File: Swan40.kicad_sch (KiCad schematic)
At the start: 82 parts, among them SW1 SW_PUSH, SW10 SW_PUSH, SW11 SW_PUSH, SW12 SW_PUSH, SW13 SW_PUSH, SW14 SW_PUSH, SW15 SW_PUSH, SW16 SW_PUSH, SW17 SW_PUSH, SW18 SW_PUSH, SW19 SW_PUSH, SW2 SW_PUSH, SW20 SW_PUSH, SW21 SW_PUSH, SW22 SW_PUSH, SW23 SW_PUSH, SW24 SW_PUSH, SW25 SW_PUSH, SW26 SW_PUSH, SW27 SW_PUSH, SW28 SW_PUSH, SW29 SW_PUSH, SW3 SW_PUSH, SW30 SW_PUSH, SW31 SW_PUSH, SW32 SW_PUSH, SW33 SW_PUSH, SW34 SW_PUSH, SW35 SW_PUSH, SW36 SW_PUSH, SW37 SW_PUSH, SW38 SW_PUSH, SW39 SW_PUSH, SW4 SW_PUSH, SW40 SW_PUSH, SW5 SW_PUSH, SW6 SW_PUSH, SW7 SW_PUSH, SW8 SW_PUSH, SW9 SW_PUSH, U1 xiao_nrf52840, U2 xiao_nrf52840

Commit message: Semi-broken 1st attempt
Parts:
- added H1, H3: BAT+, kbd:1pin_conn, symbol Mechanical:MountingHole_Pad
- added H2, H4: BAT-, kbd:1pin_conn, symbol Mechanical:MountingHole_Pad
- added SW17, SW34: SW_DPDT_x2, MSK-12C02:MSK-12C02, symbol Switch:SW_DPDT_x2
- added TP1, TP3: BOARD+, kbd:1pad_conn_board, symbol Connector:TestPoint
- added TP2, TP4: BOARD-, kbd:1pad_conn_board, symbol Connector:TestPoint
- renumbered SW17 to SW18, SW18 to SW19, SW19 to SW20, SW20 to SW21, SW21 to SW22, SW22 to SW23, SW23 to SW24, SW24 to SW25, SW25 to SW26, SW26 to SW27, SW27 to SW28, SW28 to SW29, SW29 to SW30, SW30 to SW31, SW31 to SW32, SW32 to SW33, SW33 to SW35, SW34 to SW36, SW35 to SW37, SW36 to SW38, SW37 to SW39, SW38 to SW40, SW39 to SW41, SW40 to SW42
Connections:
- net LCOL1: now also U1.3 (PA10_A2_D2); no longer U1.1 (PA02_A0_D0)
- net LCOL2: now also U1.4 (PA11_A3_D3); no longer U1.2 (PA4_A1_D1)
- net LCOL3: now also U1.5 (PA8_A4_D4_SDA); no longer U1.3 (PA10_A2_D2)
- net LCOL4: now also U1.6 (PA9_A5_D5_SCL); no longer U1.4 (PA11_A3_D3)
- net RCOL1: now also U2.3 (PA10_A2_D2); no longer U2.1 (PA02_A0_D0)
- net RCOL2: now also U2.4 (PA11_A3_D3); no longer U2.2 (PA4_A1_D1)
- net RCOL3: now also U2.5 (PA8_A4_D4_SDA); no longer U2.3 (PA10_A2_D2)
- net RCOL4: now also U2.6 (PA9_A5_D5_SCL); no longer U2.4 (PA11_A3_D3)
- new net: H4.1, TP4.1
- new net: SW34.3 (C), TP3.1
- new net: H3.1, SW34.2 (B)
- new net: H1.1, SW17.2 (B)
- new net: H2.1, TP2.1
- new net: SW17.3 (C), TP1.1
- no-connect marks 0 -> 13

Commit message: Base wiring completed
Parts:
- U1, U2: footprint xiao_nrf52840:xiao_nrf52840 -> xiao_nrf52840:xiao_nrf52840_v2
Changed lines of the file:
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@@
       (effects (font (size 1.27 1.27)))
     )
-    (property "Footprint" "xiao_nrf52840:xiao_nrf52840" (at 43.18 60.96 0)
+    (property "Footprint" "xiao_nrf52840:xiao_nrf52840_v2" (at 43.18 60.96 0)
       (effects (font (size 1.27 1.27)) hide)
     )
@@
       (effects (font (size 1.27 1.27)))
     )
-    (property "Footprint" "xiao_nrf52840:xiao_nrf52840" (at 232.41 58.42 0)
-      (effects (font (size 1.27 1.27)) hide)
-    )
+    (property "Footprint" "xiao_nrf52840:xiao_nrf52840_v2" (at 232.41 58.42 0)
+      (effects (font (size 1.27 1.27)) hide)
+    )

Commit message: Wiring complete
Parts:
- removed H1, H3: BAT+, kbd:1pin_conn, symbol Mechanical:MountingHole_Pad
- removed H2, H4: BAT-, kbd:1pin_conn, symbol Mechanical:MountingHole_Pad
- added TP1, TP5: BAT+, kbd:1pad_conn_board, symbol Connector:TestPoint
- added TP2, TP6: BAT-, kbd:1pad_conn_board, symbol Connector:TestPoint
- renumbered TP1 to TP3, TP2 to TP4, TP3 to TP7, TP4 to TP8
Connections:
- net at TP8.1: now also TP6.1
- net at SW34.2 (B): now also TP5.1
- net at SW17.2 (B): now also TP1.1
- net at TP4.1: now also TP2.1
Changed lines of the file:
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@@
+    )
+  )
+  (symbol (lib_id "Connector:TestPoint") (at 292.1 55.88 90) (unit 1)
+    (in_bom yes) (on_board yes) (dnp no) (fields_autoplaced)
+    (property "Reference" "TP5" (at 288.798 50.8 90)
+      (effects (font (size 1.27 1.27)))
+    )
+    (property "Value" "BAT+" (at 288.798 53.34 90)
+      (effects (font (size 1.27 1.27)))
+    )
+    (property "Footprint" "kbd:1pad_conn_board" (at 292.1 50.8 0)
+      (effects (font (size 1.27 1.27)) hide)
+    )
+    (property "Datasheet" "~" (at 292.1 50.8 0)
+      (effects (font (size 1.27 1.27)) hide)
+    )
+    (pin "1")
+    (instances
+      (project "Swan40"
+        (path "/b7a22810-d1fc-438f-bfc5-8d77c3380840"
+          (reference "TP5") (unit 1)
+        )
+      )
     )
   )
@@
     )
   )
-  (symbol (lib_id "Mechanical:MountingHole_Pad") (at 289.56 71.12 90) (unit 1)
-    (in_bom yes) (on_board yes) (dnp no) (fields_autoplaced)
-    (property "Reference" "H4" (at 288.29 64.77 90)
-      (effects (font (size 1.27 1.27)))
-    )
-    (property "Value" "BAT-" (at 288.29 67.31 90)
-      (effects (font (size 1.27 1.27)))
-    )
-    (property "Footprint" "kbd:1pin_conn" (at 289.56 71.12 0)
-      (effects (font (size 1.27 1.27)) hide)
-    )
-    (property "Datasheet" "~" (at 289.56 71.12 0)
-      (effects (font (size 1.27 1.27)) hide)
-    )
-    (pin "1")
-    (instances
-      (project "Swan40"
-        (path "/b7a22810-d1fc-438f-bfc5-8d77c3380840"
-          (reference "H4") (unit 1)
-        )
-      )
-    )
-  )
   (symbol (lib_id "kbd:SW_PUSH") (at 283.21 119.38 0) (unit 1)
     (in_bom yes) (on_board yes) (dnp no) (fields_autoplaced)
@@
     )
   )
+  (symbol (lib_id "Connector:TestPoint") (at 292.1 71.12 90) (unit 1)
+    (in_bom yes) (on_board yes) (dnp no) (fields_autoplaced)
+    (property "Reference" "TP6" (at 288.798 66.04 90)
+      (effects (font (size 1.27 1.27)))
+    )
+    (property "Value" "BAT-" (at 288.798 68.58 90)
+      (effects (font (size 1.27 1.27)))
+    )
+    (property "Footprint" "kbd:1pad_conn_board" (at 292.1 66.04 0)
+      (effects (font (size 1.27 1.27)) hide)
+    )
+    (property "Datasheet" "~" (at 292.1 66.04 0)
+      (effects (font (size 1.27 1.27)) hide)
+    )
+    (pin "1")
+    (instances
+      (project "Swan40"
+        (path "/b7a22810-d1fc-438f-bfc5-8d77c3380840"
+          (reference "TP6") (unit 1)
+        )
+      )
+    )
+  )
   (symbol (lib_id "Device:D") (at 86.36 111.76 90) (unit 1)
     (in_bom yes) (on_board yes) (dnp no) (fields_autoplaced)
@@
   (symbol (lib_id "Connector:TestPoint") (at 302.26 58.42 270) (unit 1)
     (in_bom yes) (on_board yes) (dnp no) (fields_autoplaced)
-    (property "Reference" "TP3" (at 307.34 57.15 90)
+    (property "Reference" "TP7" (at 307.34 57.15 90)
       (effects (font (size 1.27 1.27)) (justify left))
     )
@@
       (project "Swan40"
         (path "/b7a22810-d1fc-438f-bfc5-8d77c3380840"
-          (reference "TP3") (unit 1)
+          (reference "TP7") (unit 1)
         )
       )
@@
         (path "/b7a22810-d1fc-438f-bfc5-8d77c3380840"
           (reference "D27") (unit 1)
+        )
+      )
+    )
+  )
+  (symbol (lib_id "Connector:TestPoint") (at 114.3 74.93 90) (unit 1)
+    (in_bom yes) (on_board yes) (dnp no) (fields_autoplaced)
+    (property "Reference" "TP2" (at 110.998 69.85 90)
+      (effects (font (size 1.27 1.27)))
+    )
+    (property "Value" "BAT-" (at 110.998 72.39 90)
+      (effects (font (size 1.27 1.27)))
+    )
+    (property "Footprint" "kbd:1pad_conn_board" (at 114.3 69.85 0)
+      (effects (font (size 1.27 1.27)) hide)
+    )
+    (property "Datasheet" "~" (at 114.3 69.85 0)
+      (effects (font (size 1.27 1.27)) hide)
+    )
+    (pin "1")
+    (instances
+      (project "Swan40"
+        (path "/b7a22810-d1fc-438f-bfc5-8d77c3380840"
+          (reference "TP2") (unit 1)
         )
       )
@@
     )
   )
-  (symbol (lib_id "Mechanical:MountingHole_Pad") (at 289.56 55.88 90) (unit 1)
-    (in_bom yes) (on_board yes) (dnp no) (fields_autoplaced)
-    (property "Reference" "H3" (at 288.29 49.53 90)
-      (effects (font (size 1.27 1.27)))
-    )
-    (property "Value" "BAT+" (at 288.29 52.07 90)
-      (effects (font (size 1.27 1.27)))
-    )
-    (property "Footprint" "kbd:1pin_conn" (at 289.56 55.88 0)
-      (effects (font (size 1.27 1.27)) hide)
-    )
-    (property "Datasheet" "~" (at 289.56 55.88 0)
-      (effects (font (size 1.27 1.27)) hide)
-    )
-    (pin "1")
-    (instances
-      (project "Swan40"
-        (path "/b7a22810-d1fc-438f-bfc5-8d77c3380840"
-          (reference "H3") (unit 1)
-        )
-      )
-    )
-  )
   (symbol (lib_id "kbd:SW_PUSH") (at 300.99 105.41 0) (unit 1)
     (in_bom yes) (on_board yes) (dnp no) (fields_autoplaced)
@@
         (path "/b7a22810-d1fc-438f-bfc5-8d77c3380840"
           (reference "SW1") (unit 1)
-        )
-      )
-    )
-  )
-  (symbol (lib_id "Mechanical:MountingHole_Pad") (at 111.76 59.69 90) (unit 1)
-    (in_bom yes) (on_board yes) (dnp no) (fields_autoplaced)
-    (property "Reference" "H1" (at 110.49 53.34 90)
-      (effects (font (size 1.27 1.27)))
-    )
-    (property "Value" "BAT+" (at 110.49 55.88 90)
-      (effects (font (size 1.27 1.27)))
-    )
-    (property "Footprint" "kbd:1pin_conn" (at 111.76 59.69 0)
-      (effects (font (size 1.27 1.27)) hide)
-    )
-    (property "Datasheet" "~" (at 111.76 59.69 0)
-      (effects (font (size 1.27 1.27)) hide)
-    )
-    (pin "1")
-    (instances
-      (project "Swan40"
-        (path "/b7a22810-d1fc-438f-bfc5-8d77c3380840"
-          (reference "H1") (unit 1)
         )
       )
@@
   (symbol (lib_id "Connector:TestPoint") (at 124.46 74.93 270) (unit 1)
     (in_bom yes) (on_board yes) (dnp no) (fields_autoplaced)
-    (property "Reference" "TP2" (at 129.54 73.66 90)
+    (property "Reference" "TP4" (at 129.54 73.66 90)
       (effects (font (size 1.27 1.27)) (justify left))
     )
@@
       (project "Swan40"
         (path "/b7a22810-d1fc-438f-bfc5-8d77c3380840"
-          (reference "TP2") (unit 1)
+          (reference "TP4") (unit 1)
         )
       )
@@
   (symbol (lib_id "Connector:TestPoint") (at 124.46 62.23 270) (unit 1)
     (in_bom yes) (on_board yes) (dnp no) (fields_autoplaced)
-    (property "Reference" "TP1" (at 129.54 60.96 90)
+    (property "Reference" "TP3" (at 129.54 60.96 90)
       (effects (font (size 1.27 1.27)) (justify left))
     )
@@
       (project "Swan40"
         (path "/b7a22810-d1fc-438f-bfc5-8d77c3380840"
-          (reference "TP1") (unit 1)
+          (reference "TP3") (unit 1)
         )
       )
@@
     )
   )
+  (symbol (lib_id "Connector:TestPoint") (at 114.3 59.69 90) (unit 1)
+    (in_bom yes) (on_board yes) (dnp no) (fields_autoplaced)
+    (property "Reference" "TP1" (at 110.998 54.61 90)
+      (effects (font (size 1.27 1.27)))
+    )
+    (property "Value" "BAT+" (at 110.998 57.15 90)
+      (effects (font (size 1.27 1.27)))
+    )
+    (property "Footprint" "kbd:1pad_conn_board" (at 114.3 54.61 0)
+      (effects (font (size 1.27 1.27)) hide)
+    )
+    (property "Datasheet" "~" (at 114.3 54.61 0)
+      (effects (font (size 1.27 1.27)) hide)
+    )
+    (pin "1")
+    (instances
+      (project "Swan40"
+        (path "/b7a22810-d1fc-438f-bfc5-8d77c3380840"
+          (reference "TP1") (unit 1)
+        )
+      )
+    )
+  )
   (symbol (lib_id "kbd:SW_PUSH") (at 265.43 133.35 0) (unit 1)
     (in_bom yes) (on_board yes) (dnp no) (fields_autoplaced)
@@
     )
   )
-  (symbol (lib_id "Mechanical:MountingHole_Pad") (at 111.76 74.93 90) (unit 1)
-    (in_bom yes) (on_board yes) (dnp no) (fields_autoplaced)
-    (property "Reference" "H2" (at 110.49 68.58 90)
-      (effects (font (size 1.27 1.27)))
-    )
-    (property "Value" "BAT-" (at 110.49 71.12 90)
-      (effects (font (size 1.27 1.27)))
-    )
-    (property "Footprint" "kbd:1pin_conn" (at 111.76 74.93 0)
-      (effects (font (size 1.27 1.27)) hide)
-    )
-    (property "Datasheet" "~" (at 111.76 74.93 0)
-      (effects (font (size 1.27 1.27)) hide)
-    )
-    (pin "1")
-    (instances
-      (project "Swan40"
-        (path "/b7a22810-d1fc-438f-bfc5-8d77c3380840"
-          (reference "H2") (unit 1)
-        )
-      )
-    )
-  )
   (symbol (lib_id "Device:D") (at 86.36 139.7 90) (unit 1)
     (in_bom yes) (on_board yes) (dnp no) (fields_autoplaced)
@@
   (symbol (lib_id "Connector:TestPoint") (at 302.26 71.12 270) (unit 1)
     (in_bom yes) (on_board yes) (dnp no) (fields_autoplaced)
-    (property "Reference" "TP4" (at 307.34 69.85 90)
+    (property "Reference" "TP8" (at 307.34 69.85 90)
       (effects (font (size 1.27 1.27)) (justify left))
     )
@@
       (project "Swan40"
         (path "/b7a22810-d1fc-438f-bfc5-8d77c3380840"
-          (reference "TP4") (unit 1)
-        )
-      )
+          (reference "TP8") (unit 1)
+        )
+      )

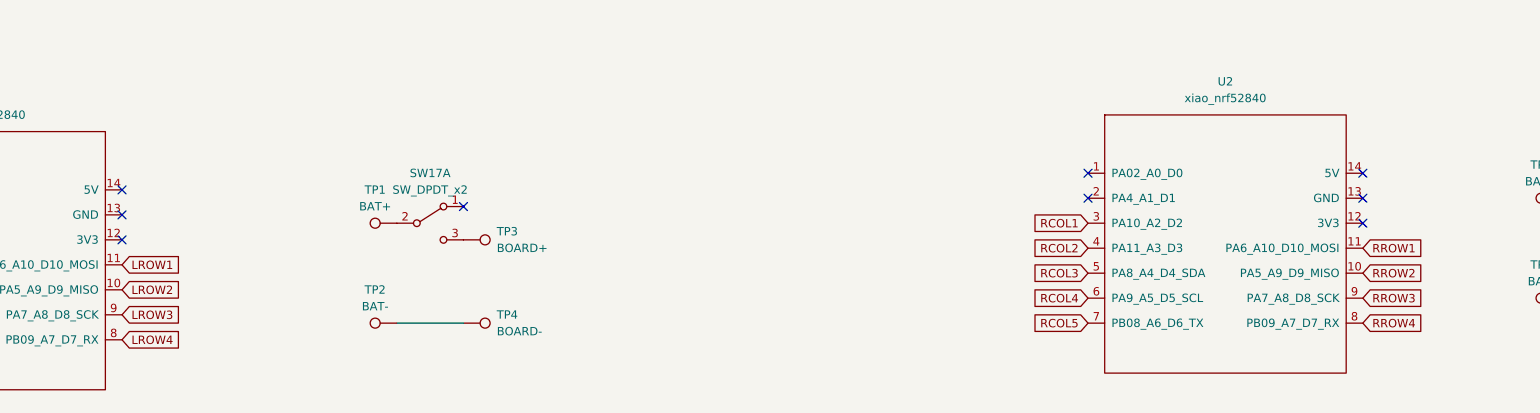
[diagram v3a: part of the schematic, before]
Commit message: Rounded + added droplets + fill zones
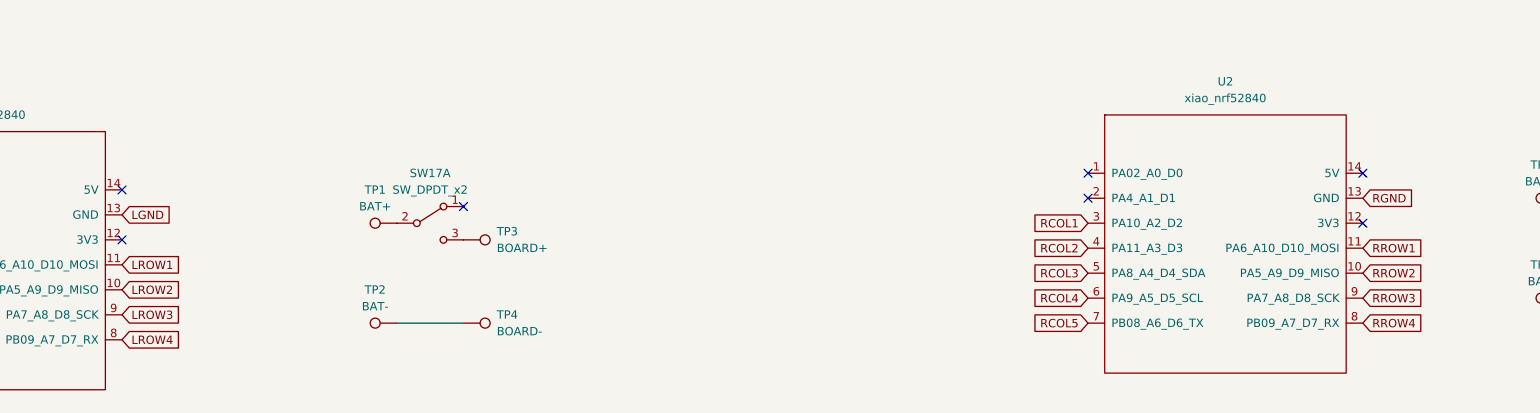
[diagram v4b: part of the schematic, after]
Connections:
- net LGND: now reaches U1.13 (GND)
- net RGND: now reaches U2.13 (GND)
- no-connect marks 13 -> 11
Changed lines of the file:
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@@
   )
   (no_connect (at 261.62 52.07))
-  (no_connect (at 72.39 58.42))
   (no_connect (at 302.26 53.34))
   (no_connect (at 124.46 57.15))
   (no_connect (at 72.39 62.23))
   (no_connect (at 30.48 54.61))
-  (no_connect (at 261.62 55.88))
   (no_connect (at 30.48 58.42))
   (no_connect (at 219.71 52.07))
@@
       (effects (font (size 1.27 1.27)) (justify left) hide)
     )
+  )
+  (global_label "RGND" (shape input) (at 261.62 55.88 0) (fields_autoplaced)
+    (effects (font (size 1.27 1.27)) (justify left))
+    (property "Intersheetrefs" "${INTERSHEET_REFS}" (at 269.7457 55.88 0)
+      (effects (font (size 1.27 1.27)) (justify left) hide)
+    )
+  )
+  (global_label "LGND" (shape input) (at 72.39 58.42 0) (fields_autoplaced)
+    (effects (font (size 1.27 1.27)) (justify left))
+    (property "Intersheetrefs" "${INTERSHEET_REFS}" (at 80.2738 58.42 0)
+      (effects (font (size 1.27 1.27)) (justify left) hide)
+    )
